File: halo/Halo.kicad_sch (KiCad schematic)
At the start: 79 parts, among them J1 USB-C 16P, J2 5V / GND alt, Q1 ALS-PT19-315C, SW1 RESET, SW2 BOOT, SW3 USER, U1 ESP32-C3-MINI-1-N4, U2 AMS1117-3.3, U3 74AHCT1G125

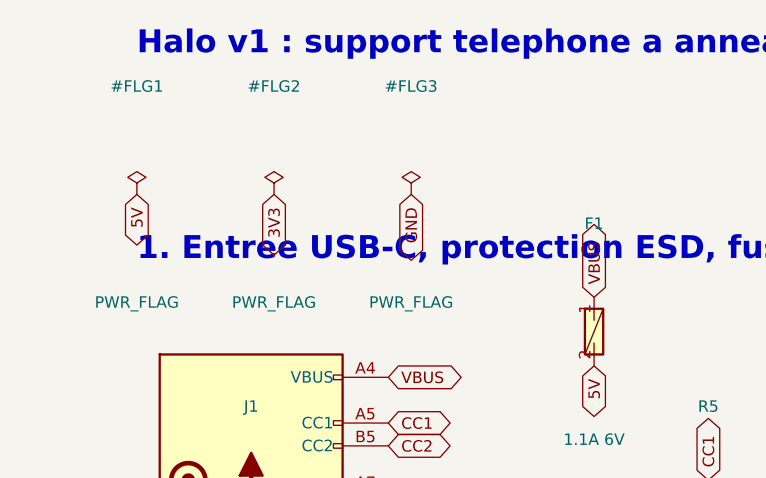
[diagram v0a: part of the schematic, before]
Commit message: Halo v1 : retrait du PWR_FLAG sur 3V3, la sortie du LDO est deja une power output (erreur ERC)
Co-Authored-By: Claude Fable 5.1 <noreply@anthropic.com>
Claude-Session: https://claude.ai/code/session_01SNPQwHsom9CDZgPKnLmdyX
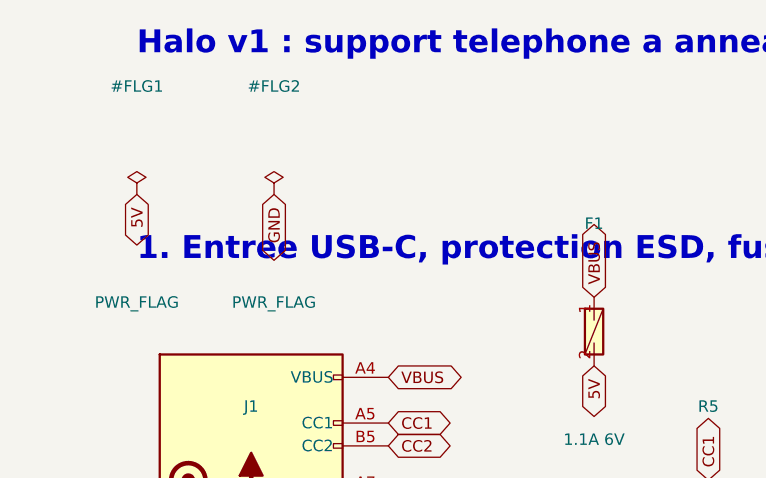
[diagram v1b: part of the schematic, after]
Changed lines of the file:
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@@
 	)
 	(symbol
-		(lib_id "power:PWR_FLAG")
-		(at 55.88 30.48 0)
-		(unit 1)
-		(exclude_from_sim no)
-		(in_bom no)
-		(on_board yes)
-		(dnp no)
-		(fields_autoplaced yes)
-		(property "Reference" "#FLG3"
-			(at 55.88 18.48 0)
-			(effects (font (size 1.27 1.27)))
-		)
-		(property "Value" "PWR_FLAG"
-			(at 55.88 42.48 0)
-			(effects (font (size 1.27 1.27)))
-		)
-		(property "Footprint" ""
-			(at 55.88 30.48 0)
-			(effects (font (size 1.27 1.27)) (hide yes))
-		)
-		(property "Datasheet" "~"
-			(at 55.88 30.48 0)
-			(effects (font (size 1.27 1.27)) (hide yes))
-		)
-		(property "Description" ""
-			(at 55.88 30.48 0)
-			(effects (font (size 1.27 1.27)) (hide yes))
-		)
-		(pin "1"
-		)
-		(instances
-			(project "Halo"
-				(path "/5c1ea366-10f2-55bd-b5fc-457e28fdddd0"
-					(reference "#FLG3")
-					(unit 1)
-				)
-			)
-		)
-	)
-	(symbol
 		(lib_id "Halo:ESP32-C3-MINI-1")
 		(at 68.58 157.48 0)
@@
 		(effects (font (size 1.27 1.27)) (justify right))
 	)
-	(global_label "3V3"
-		(shape bidirectional)
-		(at 40.64 30.48 270)
-		(effects (font (size 1.27 1.27)) (justify right))
-	)
 	(global_label "GND"
 		(shape bidirectional)
-		(at 55.88 30.48 270)
+		(at 40.64 30.48 270)
 		(effects (font (size 1.27 1.27)) (justify right))
 	)

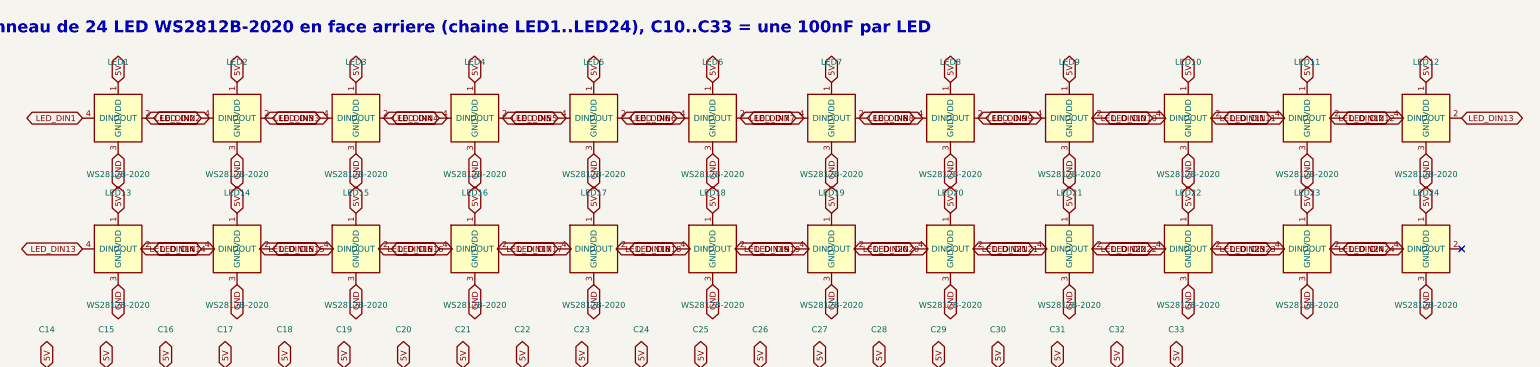
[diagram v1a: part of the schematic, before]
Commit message: Halo : empreintes ESP32-C3-MINI-1 et WS2812B-2020 d'apres les datasheets, anneau reroute, Gerbers
Verification des empreintes maison contre les datasheets avant les Gerbers :

- ESP32-C3-MINI-1 : l'empreinte "de memoire" placait les 53 broches sur le bord
  du module ; le vrai land pattern (datasheet Espressif v2.2 fig. 11-1, identique
  a espressif/kicad-libraries) a les broches en retrait a x = +/-5.9, rangees
  y = -2.2 / 7.6, masse centrale 3 x 3 (pad 49, un via par pastille), 4 pastilles
  d'angle raccordees par un court segment. Zone antenne 5.4 mm : encoche sans
  cuivre allongee a y = -26.9, keepout de routage ajuste. Table des broches
  (3-1) confirmee identique au schema.
- WS2812B-2020 Worldsemi (LCSC C965555) : brochage reel 1 DO, 2 GND, 3 DI,
  4 VDD, DI et VDD du meme cote. Symbole et empreinte (0.7 x 0.7) refaits ;
  l'anneau tourne desormais dans le sens trigonometrique depuis LED1 en bas a
  droite (impose par le brochage), data DO -> DI en segments droits, 100nF a
  r = 40. Le firmware ne presume rien de la position de LED1.
- SOT-23-5/6 et fusible 1206 aux cotes des bibliotheques KiCad 10 ; trous de
  fixation renommes MountingHole_2.2mm_M2.
- Placement : decouplage et pull-ups le long des vraies broches, F1/C7 et
  U3/R7/C8 permutes gauche/droite pour LED1 a droite. Boutons inchanges (coque).
- Librairies du projet : Halo.kicad_sym, Halo.pretty, sym-lib-table et
  fp-lib-table generes par gen_kicad_libs.py ; ERC a 0.
- Routage du centre refait par route_center.py ; drc.py 0 erreur ; kicad-cli
  pcb drc --refill-zones : 0 non connecte, 0 erreur.
- Gerbers, percage Excellon et fichier de position (kicad-cli 10.0.3) dans
  halo/GERBER_HALO et halo/Halo_GERBER.zip.

Co-Authored-By: Claude Fable 5.1 <noreply@anthropic.com>
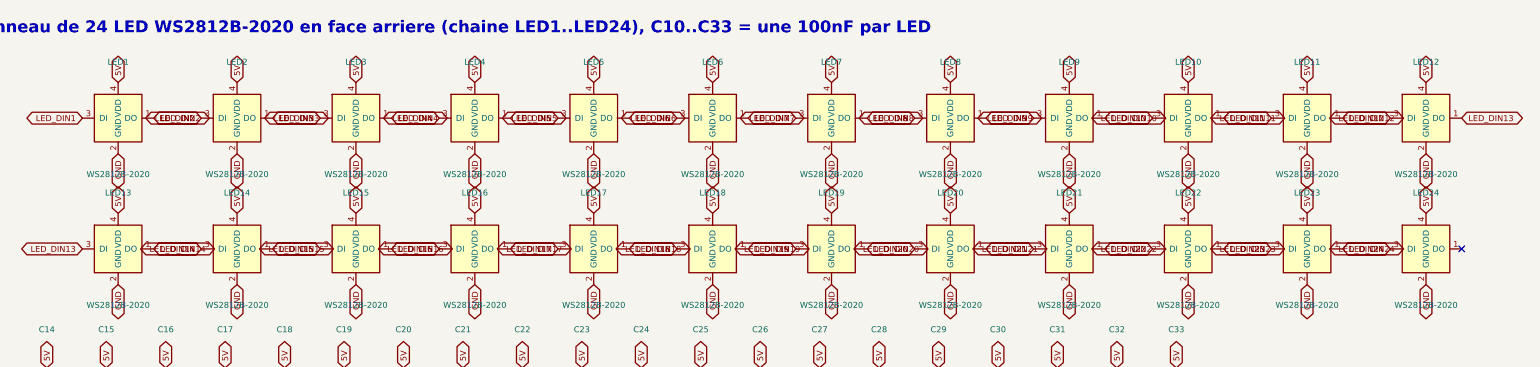
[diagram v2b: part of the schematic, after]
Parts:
- U1: footprint RF_Module:ESP32-C3-MINI-1 -> Halo:ESP32-C3-MINI-1
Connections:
- net 5V: now also LED1.4 (VDD), LED10.4 (VDD), LED11.4 (VDD), LED12.4 (VDD), LED13.4 (VDD), LED14.4 (VDD), LED15.4 (VDD), LED16.4 (VDD), LED17.4 (VDD), LED18.4 (VDD), LED19.4 (VDD), LED2.4 (VDD), LED20.4 (VDD), LED21.4 (VDD), LED22.4 (VDD), LED23.4 (VDD), LED24.4 (VDD), LED3.4 (VDD), LED4.4 (VDD), LED5.4 (VDD), LED6.4 (VDD), LED7.4 (VDD), LED8.4 (VDD), LED9.4 (VDD); no longer LED1.1 (VDD), LED10.1 (VDD), LED11.1 (VDD), LED12.1 (VDD), LED13.1 (VDD), LED14.1 (VDD), LED15.1 (VDD), LED16.1 (VDD), LED17.1 (VDD), LED18.1 (VDD), LED19.1 (VDD), LED2.1 (VDD), LED20.1 (VDD), LED21.1 (VDD), LED22.1 (VDD), LED23.1 (VDD), LED24.1 (VDD), LED3.1 (VDD), LED4.1 (VDD), LED5.1 (VDD), LED6.1 (VDD), LED7.1 (VDD), LED8.1 (VDD), LED9.1 (VDD)
- net GND: now also LED1.2 (GND), LED10.2 (GND), LED11.2 (GND), LED12.2 (GND), LED13.2 (GND), LED14.2 (GND), LED15.2 (GND), LED16.2 (GND), LED17.2 (GND), LED18.2 (GND), LED19.2 (GND), LED2.2 (GND), LED20.2 (GND), LED21.2 (GND), LED22.2 (GND), LED23.2 (GND), LED24.2 (GND), LED3.2 (GND), LED4.2 (GND), LED5.2 (GND), LED6.2 (GND), LED7.2 (GND), LED8.2 (GND), LED9.2 (GND); no longer LED1.3 (GND), LED10.3 (GND), LED11.3 (GND), LED12.3 (GND), LED13.3 (GND), LED14.3 (GND), LED15.3 (GND), LED16.3 (GND), LED17.3 (GND), LED18.3 (GND), LED19.3 (GND), LED2.3 (GND), LED20.3 (GND), LED21.3 (GND), LED22.3 (GND), LED23.3 (GND), LED24.3 (GND), LED3.3 (GND), LED4.3 (GND), LED5.3 (GND), LED6.3 (GND), LED7.3 (GND), LED8.3 (GND), LED9.3 (GND)
- net LED_DIN1: now also LED1.3 (DI); no longer LED1.4 (DIN)
- net LED_DIN10: now also LED10.3 (DI), LED9.1 (DO); no longer LED10.4 (DIN), LED9.2 (DOUT)
- net LED_DIN11: now also LED10.1 (DO), LED11.3 (DI); no longer LED10.2 (DOUT), LED11.4 (DIN)
- net LED_DIN12: now also LED11.1 (DO), LED12.3 (DI); no longer LED11.2 (DOUT), LED12.4 (DIN)
- net LED_DIN13: now also LED12.1 (DO), LED13.3 (DI); no longer LED12.2 (DOUT), LED13.4 (DIN)
- net LED_DIN14: now also LED13.1 (DO), LED14.3 (DI); no longer LED13.2 (DOUT), LED14.4 (DIN)
- net LED_DIN15: now also LED14.1 (DO), LED15.3 (DI); no longer LED14.2 (DOUT), LED15.4 (DIN)
- net LED_DIN16: now also LED15.1 (DO), LED16.3 (DI); no longer LED15.2 (DOUT), LED16.4 (DIN)
- net LED_DIN17: now also LED16.1 (DO), LED17.3 (DI); no longer LED16.2 (DOUT), LED17.4 (DIN)
- net LED_DIN18: now also LED17.1 (DO), LED18.3 (DI); no longer LED17.2 (DOUT), LED18.4 (DIN)
- net LED_DIN19: now also LED18.1 (DO), LED19.3 (DI); no longer LED18.2 (DOUT), LED19.4 (DIN)
- net LED_DIN2: now also LED1.1 (DO), LED2.3 (DI); no longer LED1.2 (DOUT), LED2.4 (DIN)
- net LED_DIN20: now also LED19.1 (DO), LED20.3 (DI); no longer LED19.2 (DOUT), LED20.4 (DIN)
- net LED_DIN21: now also LED20.1 (DO), LED21.3 (DI); no longer LED20.2 (DOUT), LED21.4 (DIN)
- net LED_DIN22: now also LED21.1 (DO), LED22.3 (DI); no longer LED21.2 (DOUT), LED22.4 (DIN)
- net LED_DIN23: now also LED22.1 (DO), LED23.3 (DI); no longer LED22.2 (DOUT), LED23.4 (DIN)
- net LED_DIN24: now also LED23.1 (DO), LED24.3 (DI); no longer LED23.2 (DOUT), LED24.4 (DIN)
- net LED_DIN3: now also LED2.1 (DO), LED3.3 (DI); no longer LED2.2 (DOUT), LED3.4 (DIN)
- net LED_DIN4: now also LED3.1 (DO), LED4.3 (DI); no longer LED3.2 (DOUT), LED4.4 (DIN)
- net LED_DIN5: now also LED4.1 (DO), LED5.3 (DI); no longer LED4.2 (DOUT), LED5.4 (DIN)
- net LED_DIN6: now also LED5.1 (DO), LED6.3 (DI); no longer LED5.2 (DOUT), LED6.4 (DIN)
- net LED_DIN7: now also LED6.1 (DO), LED7.3 (DI); no longer LED6.2 (DOUT), LED7.4 (DIN)
- net LED_DIN8: now also LED7.1 (DO), LED8.3 (DI); no longer LED7.2 (DOUT), LED8.4 (DIN)
- net LED_DIN9: now also LED8.1 (DO), LED9.3 (DI); no longer LED8.2 (DOUT), LED9.4 (DIN)
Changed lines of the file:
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@@
 			(effects (font (size 1.27 1.27)))
 		)
-		(property "Footprint" "RF_Module:ESP32-C3-MINI-1"
+		(property "Footprint" "Halo:ESP32-C3-MINI-1"
 			(at 68.58 157.48 0)
 			(effects (font (size 1.27 1.27)) (hide yes))

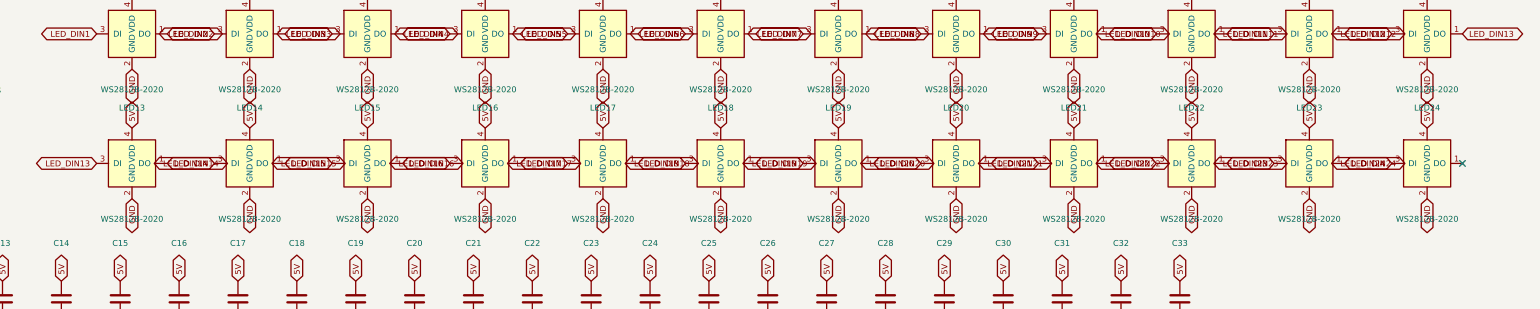
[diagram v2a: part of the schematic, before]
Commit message: Halo : le WS2812B-2020 est arrete, bascule sur le WS2812C-2020-V1 ; F1 et U3 references
JLCPCB refusait le devis : F1 sans reference LCSC (son outil cherchait alors la
description en francais, sans resultat) et 118 LEDs manquantes sur 122.

- LED1-LED24 : WS2812B-2020 (C965555) arrete par Worldsemi, 4 en stock. Remplace
  par le WS2812C-2020-V1 (C2976072, 53301 en stock) : meme boitier 2.2 x 2.0,
  meme empreinte au 0.01 mm, meme brochage 1 DO 2 GND 3 DI 4 VDD, verifie sur la
  datasheet. Il tire 5 mA par canal au lieu de 12 : halo moins lumineux, budget
  USB plus large (360 mA en blanc plein au lieu de 860). A juger sur le proto.
- F1 : SMD1206P110TF RUILON (C20801), 1.1 A / 6 V en 1206. Le MF-MSMF110-2 de
  Bourns qui etait cite en note est en 1812, il n'entre pas dans l'empreinte.
- U3 : 74AHCT1G125GV MDD (C52140417), SOT-23-5L, 5183 en stock.
- Le champ Comment de la BOM porte desormais la reference fabricant seule : c'est
  la chaine que JLCPCB envoie dans sa recherche quand il n'a pas de code LCSC.
- SCHEMA.md : budget de puissance, brochage LED et section « a confirmer » refaits.

Chaine rejouee en entier : DRC 0 erreur, BOM, CPL et PCB concordent, plus aucune
reference LCSC manquante.

Co-Authored-By: Claude Opus 5 <noreply@anthropic.com>
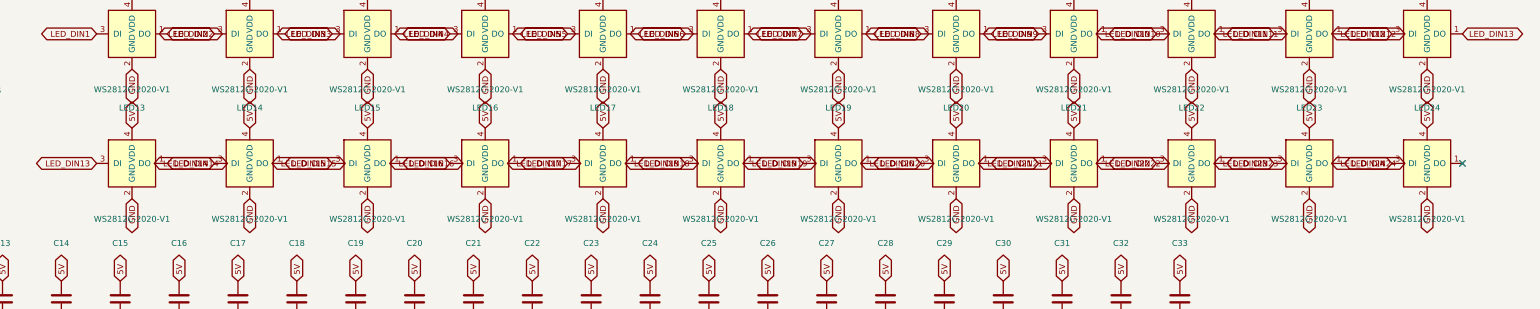
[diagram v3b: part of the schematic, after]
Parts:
- LED1, LED10, LED11, LED12, LED13, LED14, LED15, LED16, LED17, LED18, LED19, LED2, LED20, LED21, LED22, LED23, LED24, LED3, LED4, LED5, LED6, LED7, LED8, LED9: value WS2812B-2020 -> WS2812C-2020-V1
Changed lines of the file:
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@@
 			(effects (font (size 1.27 1.27)))
 		)
-		(property "Value" "WS2812B-2020"
+		(property "Value" "WS2812C-2020-V1"
 			(at 106.68 238.06 0)
 			(effects (font (size 1.27 1.27)))
@@
 			(effects (font (size 1.27 1.27)))
 		)
-		(property "Value" "WS2812B-2020"
+		(property "Value" "WS2812C-2020-V1"
 			(at 132.08 238.06 0)
 			(effects (font (size 1.27 1.27)))
@@
 			(effects (font (size 1.27 1.27)))
 		)
-		(property "Value" "WS2812B-2020"
+		(property "Value" "WS2812C-2020-V1"
 			(at 157.48 238.06 0)
 			(effects (font (size 1.27 1.27)))
@@
 			(effects (font (size 1.27 1.27)))
 		)
-		(property "Value" "WS2812B-2020"
+		(property "Value" "WS2812C-2020-V1"
 			(at 182.88 238.06 0)
 			(effects (font (size 1.27 1.27)))
@@
 			(effects (font (size 1.27 1.27)))
 		)
-		(property "Value" "WS2812B-2020"
+		(property "Value" "WS2812C-2020-V1"
 			(at 208.28 238.06 0)
 			(effects (font (size 1.27 1.27)))
@@
 			(effects (font (size 1.27 1.27)))
 		)
-		(property "Value" "WS2812B-2020"
+		(property "Value" "WS2812C-2020-V1"
 			(at 233.68 238.06 0)
 			(effects (font (size 1.27 1.27)))
@@
 			(effects (font (size 1.27 1.27)))
 		)
-		(property "Value" "WS2812B-2020"
+		(property "Value" "WS2812C-2020-V1"
 			(at 259.08 238.06 0)
 			(effects (font (size 1.27 1.27)))
@@
 			(effects (font (size 1.27 1.27)))
 		)
-		(property "Value" "WS2812B-2020"
+		(property "Value" "WS2812C-2020-V1"
 			(at 284.48 238.06 0)
 			(effects (font (size 1.27 1.27)))
@@
 			(effects (font (size 1.27 1.27)))
 		)
-		(property "Value" "WS2812B-2020"
+		(property "Value" "WS2812C-2020-V1"
 			(at 309.88 238.06 0)
 			(effects (font (size 1.27 1.27)))
@@
 			(effects (font (size 1.27 1.27)))
 		)
-		(property "Value" "WS2812B-2020"
+		(property "Value" "WS2812C-2020-V1"
 			(at 335.28 238.06 0)
 			(effects (font (size 1.27 1.27)))
@@
 			(effects (font (size 1.27 1.27)))
 		)
-		(property "Value" "WS2812B-2020"
+		(property "Value" "WS2812C-2020-V1"
 			(at 360.68 238.06 0)
 			(effects (font (size 1.27 1.27)))
@@
 			(effects (font (size 1.27 1.27)))
 		)
-		(property "Value" "WS2812B-2020"
+		(property "Value" "WS2812C-2020-V1"
 			(at 386.08 238.06 0)
 			(effects (font (size 1.27 1.27)))
@@
 			(effects (font (size 1.27 1.27)))
 		)
-		(property "Value" "WS2812B-2020"
+		(property "Value" "WS2812C-2020-V1"
 			(at 106.68 266 0)
 			(effects (font (size 1.27 1.27)))
@@
 			(effects (font (size 1.27 1.27)))
 		)
-		(property "Value" "WS2812B-2020"
+		(property "Value" "WS2812C-2020-V1"
 			(at 132.08 266 0)
 			(effects (font (size 1.27 1.27)))
@@
 			(effects (font (size 1.27 1.27)))
 		)
-		(property "Value" "WS2812B-2020"
+		(property "Value" "WS2812C-2020-V1"
 			(at 157.48 266 0)
 			(effects (font (size 1.27 1.27)))
@@
 			(effects (font (size 1.27 1.27)))
 		)
-		(property "Value" "WS2812B-2020"
+		(property "Value" "WS2812C-2020-V1"
 			(at 182.88 266 0)
 			(effects (font (size 1.27 1.27)))
@@
 			(effects (font (size 1.27 1.27)))
 		)
-		(property "Value" "WS2812B-2020"
+		(property "Value" "WS2812C-2020-V1"
 			(at 208.28 266 0)
 			(effects (font (size 1.27 1.27)))
@@
 			(effects (font (size 1.27 1.27)))
 		)
-		(property "Value" "WS2812B-2020"
+		(property "Value" "WS2812C-2020-V1"
 			(at 233.68 266 0)
 			(effects (font (size 1.27 1.27)))
@@
 			(effects (font (size 1.27 1.27)))
 		)
-		(property "Value" "WS2812B-2020"
+		(property "Value" "WS2812C-2020-V1"
 			(at 259.08 266 0)
 			(effects (font (size 1.27 1.27)))
@@
 			(effects (font (size 1.27 1.27)))
 		)
-		(property "Value" "WS2812B-2020"
+		(property "Value" "WS2812C-2020-V1"
 			(at 284.48 266 0)
 			(effects (font (size 1.27 1.27)))
@@
 			(effects (font (size 1.27 1.27)))
 		)
-		(property "Value" "WS2812B-2020"
+		(property "Value" "WS2812C-2020-V1"
 			(at 309.88 266 0)
 			(effects (font (size 1.27 1.27)))
@@
 			(effects (font (size 1.27 1.27)))
 		)
-		(property "Value" "WS2812B-2020"
+		(property "Value" "WS2812C-2020-V1"
 			(at 335.28 266 0)
 			(effects (font (size 1.27 1.27)))
@@
 			(effects (font (size 1.27 1.27)))
 		)
-		(property "Value" "WS2812B-2020"
+		(property "Value" "WS2812C-2020-V1"
 			(at 360.68 266 0)
 			(effects (font (size 1.27 1.27)))
@@
 			(effects (font (size 1.27 1.27)))
 		)
-		(property "Value" "WS2812B-2020"
+		(property "Value" "WS2812C-2020-V1"
 			(at 386.08 266 0)
 			(effects (font (size 1.27 1.27)))
